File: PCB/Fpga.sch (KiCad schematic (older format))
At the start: 51 parts

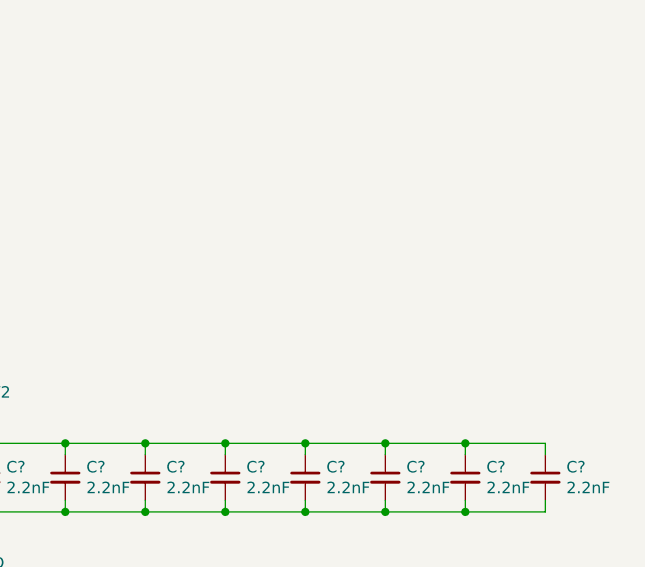
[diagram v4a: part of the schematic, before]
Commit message: Add decoupling for other FPGA supplies
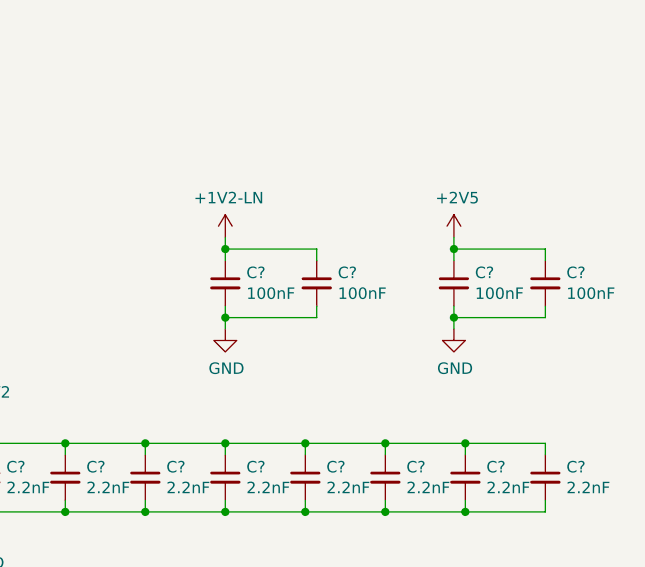
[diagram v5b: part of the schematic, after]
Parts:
- added C? (x4): 100nF, Capacitors_SMD:C_0603_HandSoldering, symbol Device:C_Small
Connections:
- net +1V2-LN: now also C?.1, C?.1
- net +2V5: now also C?.1, C?.1
- net GND: now also C?.2, C?.2, C?.2, C?.2
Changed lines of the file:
@@
 Wire Wire Line
 	5750 6250 5800 6250
+$Comp
+L power:+2V5 #PWR?
+U 1 1 5DFECD1A
+P 10500 2500
+F 0 "#PWR?" H 10500 2350 50  0001 C CNN
+F 1 "+2V5" H 10515 2673 50  0000 C CNN
+F 2 "" H 10500 2500 50  0001 C CNN
+F 3 "" H 10500 2500 50  0001 C CNN
+	1    10500 2500
+	1    0    0    -1
+$EndComp
+$Comp
+L power:GND #PWR?
+U 1 1 5DFEE032
+P 10500 2900
+F 0 "#PWR?" H 10500 2650 50  0001 C CNN
+F 1 "GND" H 10505 2727 50  0000 C CNN
+F 2 "" H 10500 2900 50  0001 C CNN
+F 3 "" H 10500 2900 50  0001 C CNN
+	1    10500 2900
+	1    0    0    -1
+$EndComp
+$Comp
+L Device:C_Small C?
+U 1 1 5DFEF761
+P 10900 2700
+F 0 "C?" H 10992 2746 50  0000 L CNN
+F 1 "100nF" H 10992 2655 50  0000 L CNN
+F 2 "Capacitors_SMD:C_0603_HandSoldering" H 10900 2700 50  0001 C CNN
+F 3 "https://www.digikey.ca/product-detail/en/w-rth-elektronik/885012206020/732-7939-1-ND/5454566" H 10900 2700 50  0001 C CNN
+	1    10900 2700
+	1    0    0    -1
+$EndComp
+Wire Wire Line
+	10500 2800 10500 2850
+Wire Wire Line
+	10500 2600 10500 2550
+Wire Wire Line
+	10500 2550 10900 2550
+Wire Wire Line
+	10900 2550 10900 2600
+Connection ~ 10500 2550
+Wire Wire Line
+	10500 2550 10500 2500
+Wire Wire Line
+	10900 2800 10900 2850
+Wire Wire Line
+	10900 2850 10500 2850
+Connection ~ 10500 2850
+Wire Wire Line
+	10500 2850 10500 2900
+$Comp
+L Parts:+1V2-LN #PWR?
+U 1 1 5E042119
+P 9500 2500
+F 0 "#PWR?" H 9500 2350 50  0001 C CNN
+F 1 "+1V2-LN" H 9515 2673 50  0000 C CNN
+F 2 "" H 9500 2500 50  0001 C CNN
+F 3 "" H 9500 2500 50  0001 C CNN
+	1    9500 2500
+	1    0    0    -1
+$EndComp
+$Comp
+L power:GND #PWR?
+U 1 1 5E04295B
+P 9500 2900
+F 0 "#PWR?" H 9500 2650 50  0001 C CNN
+F 1 "GND" H 9505 2727 50  0000 C CNN
+F 2 "" H 9500 2900 50  0001 C CNN
+F 3 "" H 9500 2900 50  0001 C CNN
+	1    9500 2900
+	1    0    0    -1
+$EndComp
+$Comp
+L Device:C_Small C?
+U 1 1 5E042D0D
+P 9500 2700
+F 0 "C?" H 9592 2746 50  0000 L CNN
+F 1 "100nF" H 9592 2655 50  0000 L CNN
+F 2 "Capacitors_SMD:C_0603_HandSoldering" H 9500 2700 50  0001 C CNN
+F 3 "https://www.digikey.ca/product-detail/en/w-rth-elektronik/885012206020/732-7939-1-ND/5454566" H 9500 2700 50  0001 C CNN
+	1    9500 2700
+	1    0    0    -1
+$EndComp
+$Comp
+L Device:C_Small C?
+U 1 1 5E043573
+P 9900 2700
+F 0 "C?" H 9992 2746 50  0000 L CNN
+F 1 "100nF" H 9992 2655 50  0000 L CNN
+F 2 "Capacitors_SMD:C_0603_HandSoldering" H 9900 2700 50  0001 C CNN
+F 3 "https://www.digikey.ca/product-detail/en/w-rth-elektronik/885012206020/732-7939-1-ND/5454566" H 9900 2700 50  0001 C CNN
+	1    9900 2700
+	1    0    0    -1
+$EndComp
+Wire Wire Line
+	9500 2500 9500 2550
+Wire Wire Line
+	9500 2550 9900 2550
+Wire Wire Line
+	9900 2550 9900 2600
+Connection ~ 9500 2550
+Wire Wire Line
+	9500 2550 9500 2600
+Wire Wire Line
+	9500 2800 9500 2850
+Wire Wire Line
+	9500 2850 9900 2850
+Wire Wire Line
+	9900 2850 9900 2800
+Connection ~ 9500 2850
+Wire Wire Line
+	9500 2850 9500 2900
+$Comp
+L Device:C_Small C?
+U 1 1 5E09336F
+P 10500 2700
+F 0 "C?" H 10592 2746 50  0000 L CNN
+F 1 "100nF" H 10592 2655 50  0000 L CNN
+F 2 "Capacitors_SMD:C_0603_HandSoldering" H 10500 2700 50  0001 C CNN
+F 3 "https://www.digikey.ca/product-detail/en/w-rth-elektronik/885012206020/732-7939-1-ND/5454566" H 10500 2700 50  0001 C CNN
+	1    10500 2700
+	1    0    0    -1
+$EndComp
 $EndSCHEMATC

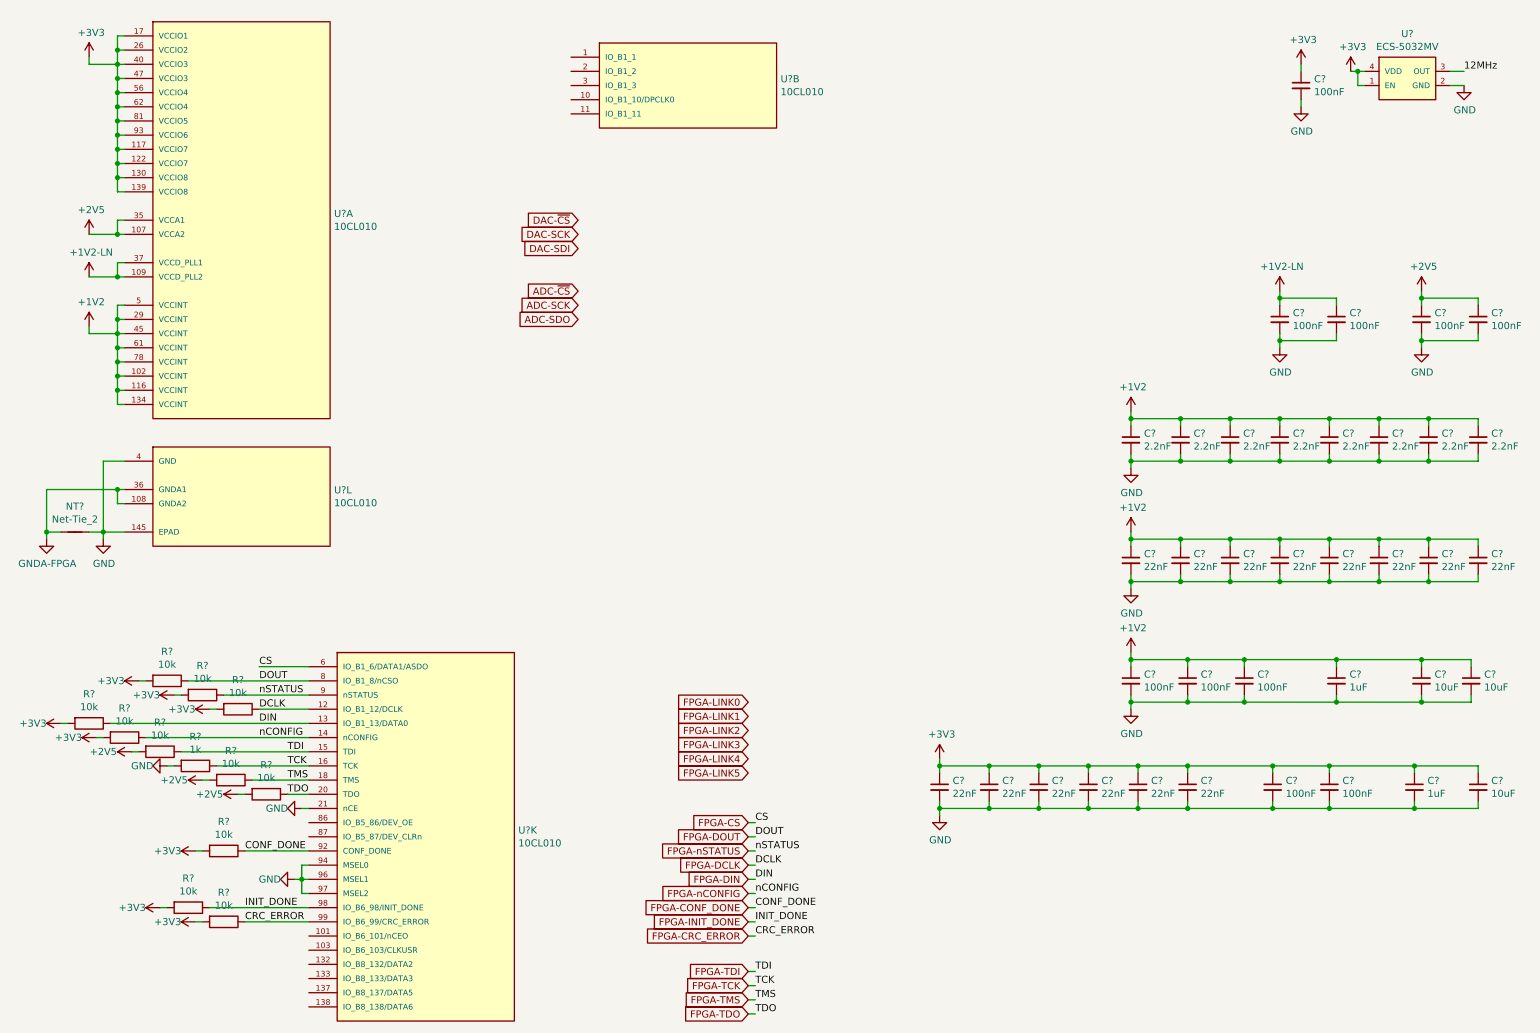
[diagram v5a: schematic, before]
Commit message: Connect signals to FPGA, normalize appearance of footprints
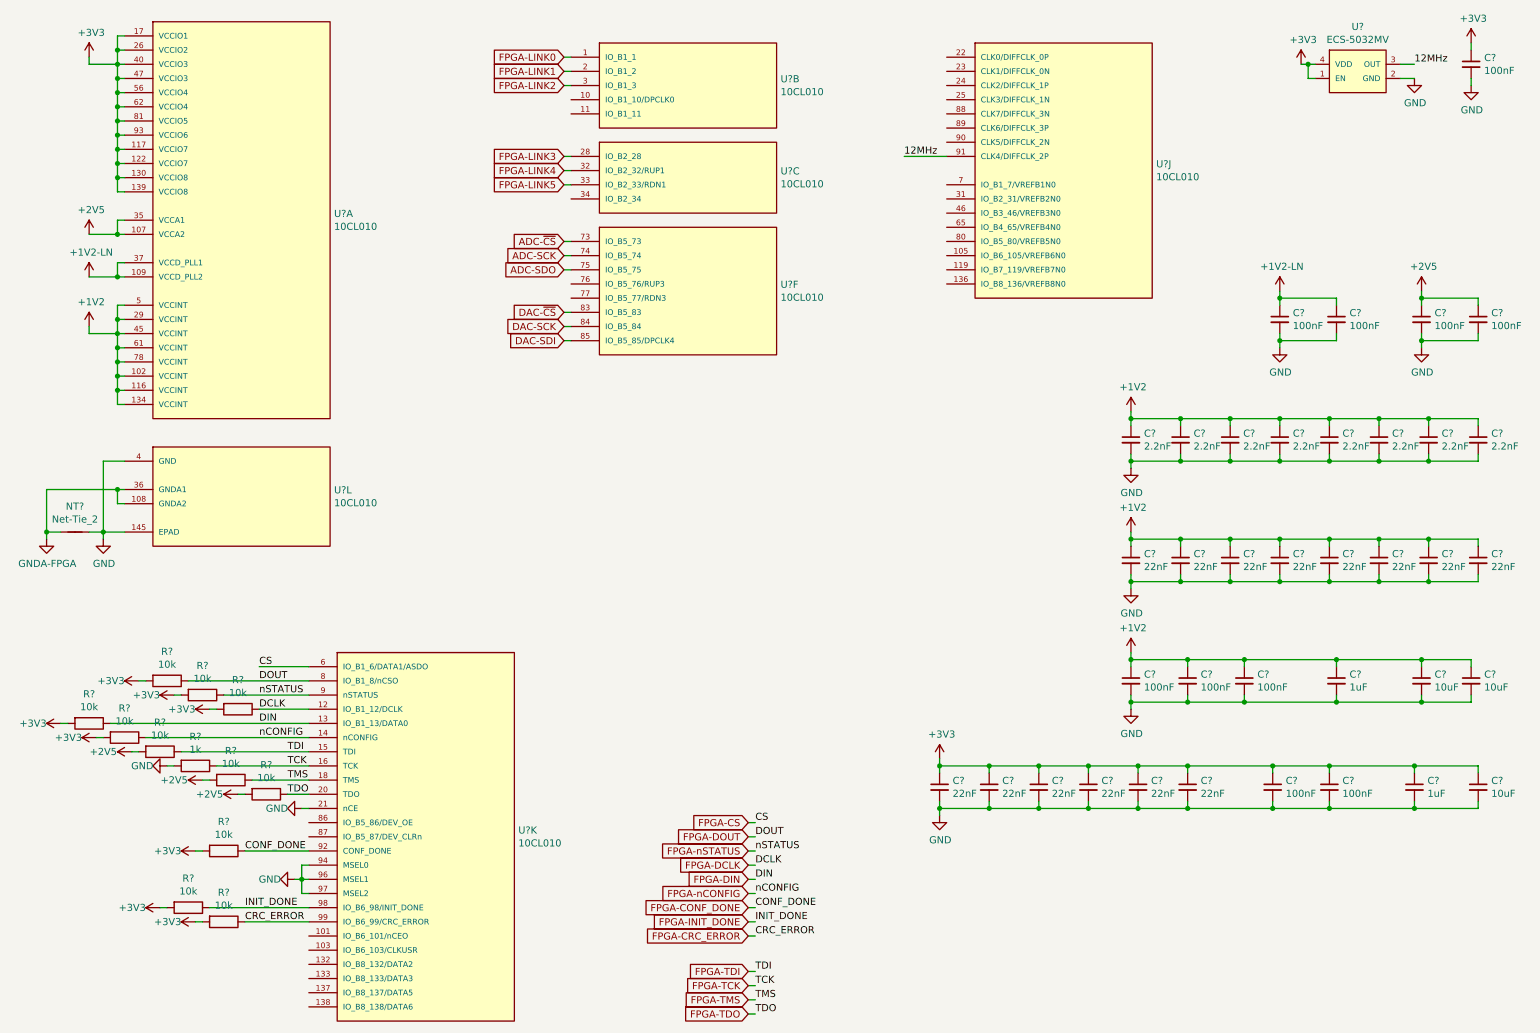
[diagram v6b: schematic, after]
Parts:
- added U? (x3): 10CL010, Parts:EQFP144-PAD, symbol Parts:10CL010
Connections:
- net 12MHz: now also U?.91 (CLK4/DIFFCLK_2P)
- net ADC-SCK: now also U?.74 (IO_B5_74)
- net ADC-SDO: now also U?.75 (IO_B5_75)
- net ADC-~CS: now also U?.73 (IO_B5_73)
- net DAC-SCK: now also U?.84 (IO_B5_84)
- net DAC-SDI: now also U?.85 (IO_B5_85/DPCLK4)
- net DAC-~CS: now also U?.83 (IO_B5_83)
- net FPGA-LINK0: now also U?.1 (IO_B1_1)
- net FPGA-LINK1: now also U?.2 (IO_B1_2)
- net FPGA-LINK2: now also U?.3 (IO_B1_3)
- net FPGA-LINK3: now also U?.28 (IO_B2_28)
- net FPGA-LINK4: now also U?.32 (IO_B2_32/RUP1)
- net FPGA-LINK5: now also U?.33 (IO_B2_33/RDN1)
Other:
- moved on the sheet: C?, U?
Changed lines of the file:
@@
 L Parts:ECS-5032MV U?
 U 1 1 5DD22CF7
-P 10400 1000
-F 0 "U?" H 10400 1315 50  0000 C CNN
-F 1 "ECS-5032MV" H 10400 1224 50  0000 C CNN
-F 2 "Parts:ECS-5032MV" H 10400 700 50  0001 C CNN
-F 3 "https://ecsxtal.com/ecs-5032mv" H 10400 600 50  0001 C CNN
-	1    10400 1000
+P 10050 950
+F 0 "U?" H 10050 1265 50  0000 C CNN
+F 1 "ECS-5032MV" H 10050 1174 50  0000 C CNN
+F 2 "Parts:ECS-5032MV" H 10050 650 50  0001 C CNN
+F 3 "https://ecsxtal.com/ecs-5032mv" H 10050 550 50  0001 C CNN
+	1    10050 950
 	1    0    0    -1
 $EndComp
@@
 Wire Wire Line
 	1300 2300 1300 2400
-Text GLabel 4550 2000 0    50   Input ~ 0
+Text GLabel 4450 2650 0    50   Input ~ 0
 DAC-~CS
-Text GLabel 4550 2100 0    50   Input ~ 0
+Text GLabel 4450 2750 0    50   Input ~ 0
 DAC-SCK
-Text GLabel 4550 2200 0    50   Input ~ 0
+Text GLabel 4450 2850 0    50   Input ~ 0
 DAC-SDI
-Text GLabel 4550 2500 0    50   Input ~ 0
+Text GLabel 4450 2150 0    50   Input ~ 0
 ADC-~CS
-Text GLabel 4550 2600 0    50   Input ~ 0
+Text GLabel 4450 2250 0    50   Input ~ 0
 ADC-SCK
-Text GLabel 4550 2700 0    50   Input ~ 0
+Text GLabel 4450 2350 0    50   Input ~ 0
 ADC-SDO
 $Comp
@@
 Wire Wire Line
 	5750 6350 5800 6350
-Text GLabel 5750 5400 0    50   Input ~ 0
+Text GLabel 4450 850  0    50   Input ~ 0
 FPGA-LINK0
-Text GLabel 5750 5500 0    50   Input ~ 0
+Text GLabel 4450 950  0    50   Input ~ 0
 FPGA-LINK1
-Text GLabel 5750 5600 0    50   Input ~ 0
+Text GLabel 4450 1050 0    50   Input ~ 0
 FPGA-LINK2
-Text GLabel 5750 5700 0    50   Input ~ 0
+Text GLabel 4450 1550 0    50   Input ~ 0
 FPGA-LINK3
-Text GLabel 5750 5800 0    50   Input ~ 0
+Text GLabel 4450 1650 0    50   Input ~ 0
 FPGA-LINK4
 $Comp
 L power:+3V3 #PWR?
 U 1 1 5DD97BF5
-P 10000 950
-F 0 "#PWR?" H 10000 800 50  0001 C CNN
-F 1 "+3V3" H 10015 1123 50  0000 C CNN
-F 2 "" H 10000 950 50  0001 C CNN
-F 3 "" H 10000 950 50  0001 C CNN
-	1    10000 950
-	1    0    0    -1
-$EndComp
-Wire Wire Line
-	10000 950  10050 950
+P 9650 900
+F 0 "#PWR?" H 9650 750 50  0001 C CNN
+F 1 "+3V3" H 9665 1073 50  0000 C CNN
+F 2 "" H 9650 900 50  0001 C CNN
+F 3 "" H 9650 900 50  0001 C CNN
+	1    9650 900
+	1    0    0    -1
+$EndComp
 $Comp
 L power:GND #PWR?
 U 1 1 5DD9CD01
-P 10800 1050
-F 0 "#PWR?" H 10800 800 50  0001 C CNN
-F 1 "GND" H 10805 877 50  0000 C CNN
-F 2 "" H 10800 1050 50  0001 C CNN
-F 3 "" H 10800 1050 50  0001 C CNN
-	1    10800 1050
-	1    0    0    -1
-$EndComp
-Wire Wire Line
-	10700 1050 10800 1050
-Text Label 10800 950  0    50   ~ 0
+P 10450 1000
+F 0 "#PWR?" H 10450 750 50  0001 C CNN
+F 1 "GND" H 10455 827 50  0000 C CNN
+F 2 "" H 10450 1000 50  0001 C CNN
+F 3 "" H 10450 1000 50  0001 C CNN
+	1    10450 1000
+	1    0    0    -1
+$EndComp
+Wire Wire Line
+	10350 1000 10450 1000
+Text Label 10450 900  0    50   ~ 0
 12MHz
 Wire Wire Line
-	10700 950  10800 950
-Wire Wire Line
-	10050 950  10050 1050
-Wire Wire Line
-	10050 1050 10100 1050
-Connection ~ 10050 950
-Wire Wire Line
-	10050 950  10100 950
+	10350 900  10450 900
 $Comp
 L Parts:+1V2-LN #PWR?
@@
 L Device:C_Small C?
 U 1 1 5DD852FA
-P 9650 1050
-F 0 "C?" H 9742 1096 50  0000 L CNN
-F 1 "100nF" H 9742 1005 50  0000 L CNN
-F 2 "Capacitors_SMD:C_0603_HandSoldering" H 9650 1050 50  0001 C CNN
-F 3 "https://www.digikey.ca/product-detail/en/w-rth-elektronik/885012206020/732-7939-1-ND/5454566" H 9650 1050 50  0001 C CNN
-	1    9650 1050
+P 10850 900
+F 0 "C?" H 10942 946 50  0000 L CNN
+F 1 "100nF" H 10942 855 50  0000 L CNN
+F 2 "Capacitors_SMD:C_0603_HandSoldering" H 10850 900 50  0001 C CNN
+F 3 "https://www.digikey.ca/product-detail/en/w-rth-elektronik/885012206020/732-7939-1-ND/5454566" H 10850 900 50  0001 C CNN
+	1    10850 900
 	1    0    0    -1
 $EndComp
@@
 L power:+3V3 #PWR?
 U 1 1 5DD89B39
-P 9650 900
-F 0 "#PWR?" H 9650 750 50  0001 C CNN
-F 1 "+3V3" H 9665 1073 50  0000 C CNN
-F 2 "" H 9650 900 50  0001 C CNN
-F 3 "" H 9650 900 50  0001 C CNN
-	1    9650 900
-	1    0    0    -1
-$EndComp
-Wire Wire Line
-	9650 900  9650 950
+P 10850 750
+F 0 "#PWR?" H 10850 600 50  0001 C CNN
+F 1 "+3V3" H 10865 923 50  0000 C CNN
+F 2 "" H 10850 750 50  0001 C CNN
+F 3 "" H 10850 750 50  0001 C CNN
+	1    10850 750
+	1    0    0    -1
+$EndComp
+Wire Wire Line
+	10850 750  10850 800
 $Comp
 L power:GND #PWR?
 U 1 1 5DD8DD81
-P 9650 1200
-F 0 "#PWR?" H 9650 950 50  0001 C CNN
-F 1 "GND" H 9655 1027 50  0000 C CNN
-F 2 "" H 9650 1200 50  0001 C CNN
-F 3 "" H 9650 1200 50  0001 C CNN
-	1    9650 1200
-	1    0    0    -1
-$EndComp
-Wire Wire Line
-	9650 1150 9650 1200
-Text GLabel 5750 5900 0    50   Input ~ 0
+P 10850 1050
+F 0 "#PWR?" H 10850 800 50  0001 C CNN
+F 1 "GND" H 10855 877 50  0000 C CNN
+F 2 "" H 10850 1050 50  0001 C CNN
+F 3 "" H 10850 1050 50  0001 C CNN
+	1    10850 1050
+	1    0    0    -1
+$EndComp
+Wire Wire Line
+	10850 1000 10850 1050
+Text GLabel 4450 1750 0    50   Input ~ 0
 FPGA-LINK5
 $Comp
@@
 	1    0    0    -1
 $EndComp
+$Comp
+L Parts:10CL010 U?
+U 6 1 5E0ED08E
+P 4700 2050
+F 0 "U?" H 5978 1646 50  0000 L CNN
+F 1 "10CL010" H 5978 1555 50  0000 L CNN
+F 2 "Parts:EQFP144-PAD" H 5550 2100 50  0001 L BNN
+F 3 "https://www.intel.com/content/www/us/en/programmable/products/fpga/cyclone-series/cyclone-10/cyclone-10-lp/support.html" H 4700 2050 50  0001 C CNN
+	6    4700 2050
+	1    0    0    -1
+$EndComp
+Wire Wire Line
+	4450 2150 4500 2150
+Wire Wire Line
+	4500 2250 4450 2250
+Wire Wire Line
+	4450 2350 4500 2350
+Wire Wire Line
+	4500 2650 4450 2650
+Wire Wire Line
+	4450 2750 4500 2750
+Wire Wire Line
+	4500 2850 4450 2850
+$Comp
+L Parts:10CL010 U?
+U 10 1 5E1E1598
+P 7350 750
+F 0 "U?" H 8628 -104 50  0000 L CNN
+F 1 "10CL010" H 8628 -195 50  0000 L CNN
+F 2 "Parts:EQFP144-PAD" H 8200 800 50  0001 L BNN
+F 3 "https://www.intel.com/content/www/us/en/programmable/products/fpga/cyclone-series/cyclone-10/cyclone-10-lp/support.html" H 7350 750 50  0001 C CNN
+	10   7350 750
+	1    0    0    -1
+$EndComp
+Text Label 6850 1550 0    50   ~ 0
+12MHz
+Wire Wire Line
+	6850 1550 7150 1550
+Wire Wire Line
+	9650 900  9700 900
+Wire Wire Line
+	9700 900  9700 1000
+Wire Wire Line
+	9700 1000 9750 1000
+Connection ~ 9700 900
+Wire Wire Line
+	9700 900  9750 900
+$Comp
+L Parts:10CL010 U?
+U 3 1 5E2AA860
+P 4700 1450
+F 0 "U?" H 5978 1246 50  0000 L CNN
+F 1 "10CL010" H 5978 1155 50  0000 L CNN
+F 2 "Parts:EQFP144-PAD" H 5550 1500 50  0001 L BNN
+F 3 "https://www.intel.com/content/www/us/en/programmable/products/fpga/cyclone-series/cyclone-10/cyclone-10-lp/support.html" H 4700 1450 50  0001 C CNN
+	3    4700 1450
+	1    0    0    -1
+$EndComp
+Wire Wire Line
+	4450 850  4500 850
+Wire Wire Line
+	4450 950  4500 950
+Wire Wire Line
+	4500 1050 4450 1050
+Wire Wire Line
+	4450 1550 4500 1550
+Wire Wire Line
+	4500 1650 4450 1650
+Wire Wire Line
+	4450 1750 4500 1750
 $EndSCHEMATC
